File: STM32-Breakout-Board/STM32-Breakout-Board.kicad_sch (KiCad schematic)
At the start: 1 part, among them U1 stm32l443cct6

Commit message: Schematic and Layout update
Finished the first draft of the Schematic.
Started layout
Edited some components
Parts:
- added C1, C2, C3, C4, C9: 100n, Capacitor_SMD:C_0402_1005Metric, symbol Device:C
- added C10, C11: 10p, Capacitor_SMD:C_0402_1005Metric, symbol Device:C
- added C12, C13: 22u, Capacitor_SMD:C_0805_2012Metric, symbol Device:C
- added C5: 10u, Capacitor_SMD:C_0805_2012Metric, symbol Device:C
- added C6: 10n, Capacitor_SMD:C_0402_1005Metric, symbol Device:C
- added C7, C8: 1u, Capacitor_SMD:C_0603_1608Metric, symbol Device:C
- added D1: RED, LED_SMD:LED_0603_1608Metric, symbol Device:LED
- added FB1: 120R, Inductor_SMD:L_0603_1608Metric, symbol Device:FerriteBead
- added H1, H2, H3, H4: MountingHole, MountingHole:MountingHole_2.5mm, symbol Mechanical:MountingHole
- added J1: USB_B_Micro, Connector_USB:USB_Micro-B_Wuerth_629105150521, symbol Connector:USB_B_Micro
- added J2: Conn_01x04_Pin, Connector_PinSocket_2.00mm:PinSocket_1x04_P2.00mm_Vertical, symbol Connector:Conn_01x04_Pin
- added J3, J4: Conn_01x10_Socket, Connector_PinSocket_2.00mm:PinSocket_1x10_P2.00mm_Vertical, symbol Connector:Conn_01x10_Socket
- added R1, R2, R3, R4, R5: 1k5, Resistor_SMD:R_0402_1005Metric, symbol Device:R
- added SW1: SW_SPDT, Button_Switch_SMD:SW_SPDT_PCM12, symbol Switch:SW_SPDT
- added U2: MCP1799T-3302H/DB, BBSTM32_pcblib:SOT-223 b, symbol BBSTM32_symlib:MCP1799T-3302H/DB
- added Y1: Crystal_GND24, Crystal:Crystal_SMD_3225-4Pin_3.2x2.5mm, symbol Device:Crystal_GND24
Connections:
- net +3.3V: now reaches U1.1 (VBAT)
- net +3.3V: now also U1.24 (VDD), U1.36 (VDDUSB), U1.48 (VDD), C1.1, C13.1, C2.1, C3.1, C4.1, C5.1, C8.1, FB1.2, J2.1 (Pin_1), R2.2, R3.2, R4.1, R5.2, SW1.3 (C), U2.3 (VOUT)
- net PA0: now reaches U1.10 (PA0)
- net PA0: now also J3.1 (Pin_1)
- net PA1: now reaches U1.11 (PA1)
- net PA1: now also J3.2 (Pin_2)
- net PA2: now reaches U1.12 (PA2)
- net PA2: now also J3.3 (Pin_3)
- net PA3: now reaches U1.13 (PA3)
- net PA3: now also J3.4 (Pin_4)
- net PA4: now reaches U1.14 (PA4)
- net PA4: now also J3.5 (Pin_5)
- net PA5: now reaches U1.15 (PA5)
- net PA5: now also J3.6 (Pin_6)
- net PA6: now reaches U1.16 (PA6)
- net PA6: now also J3.7 (Pin_7)
- net PA7: now reaches U1.17 (PA7)
- net PA7: now also J3.8 (Pin_8)
- net PB0: now reaches U1.18 (PB0)
- net PB0: now also J4.1 (Pin_1)
- net PB1: now reaches U1.19 (PB1)
- net PB1: now also J4.2 (Pin_2)
- net PB2: now reaches U1.20 (PB2)
- net PB2: now also J4.3 (Pin_3)
- net I2C_SCL: now reaches U1.21 (PB10)
- net I2C_SCL: now also J2.2 (Pin_2), R2.1
- net I2C_SDA: now reaches U1.22 (PB11)
- net I2C_SDA: now also J2.3 (Pin_3), R3.1
- net GND: now reaches U1.23 (VSS)
- net GND: now also U1.35 (VSS), U1.47 (VSS), U1.8 (VSSA), C1.2, C10.2, C11.2, C12.2, C13.2, C2.2, C3.2, C4.2, C5.2, C6.2, C7.2, C8.2, C9.1, D1.1 (K), J1.5 (GND), J2.4 (Pin_4), SW1.1 (A), U2.2 (GND), Y1.2 (G), Y1.4 (G)
- net PA8: now reaches U1.29 (PA8)
- net PA8: now also J3.9 (Pin_9)
- net PA9: now reaches U1.30 (PA9)
- net PA9: now also J3.10 (Pin_10)
- net USB_D-: now reaches U1.32 (PA11)
- net USB_D-: now also J1.2 (D-)
- net USB_D+: now reaches U1.33 (PA12)
- net USB_D+: now also J1.3 (D+), R5.1
- net PB3: now reaches U1.39 (PB3)
- net PB3: now also J4.4 (Pin_4)
- net PB4: now reaches U1.40 (PB4)
- net PB4: now also J4.5 (Pin_5)
- net PB5: now reaches U1.41 (PB5)
- net PB5: now also J4.6 (Pin_6)
- net PB6: now reaches U1.42 (PB6)
- net PB6: now also J4.7 (Pin_7)
- net PB7: now reaches U1.43 (PB7)
- net PB7: now also J4.8 (Pin_8)
- net BOOT0: now reaches U1.44 (BOOT0)
- net BOOT0: now also R1.2
- net PB8: now reaches U1.45 (PB8)
- net PB8: now also J4.9 (Pin_9)
- net PB9: now reaches U1.46 (PB9)
- net PB9: now also J4.10 (Pin_10)
- net HSE_IN: now reaches U1.5 (PH0)
- net HSE_IN: now also C10.1, Y1.1
- net HSE_OUT: now reaches U1.6 (PH1)
- net HSE_OUT: now also C11.1, Y1.3
- net NRST: now reaches U1.7 (NRST)
- net NRST: now also C9.2
- net +3.3VA: now reaches U1.9 (VDDA)
- net +3.3VA: now also C6.1, C7.1, FB1.1
- new net LED_A: D1.2 (A), R4.2
- new net SW_BOOT0: R1.1, SW1.2 (B)
- new net VBUS: C12.1, J1.1 (VBUS), U2.1 (VIN)
- no-connect marks 0 -> 13
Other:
- note added: "I2C and USB"
- note added: "Microcontroller"
- note added: "Mounting Holes"
- note added: "Power Supply"
- note added: "STM32 Breakout Board"
- company: (none) -> SaintDTS
- title: (none) -> STM32 Breakout Board

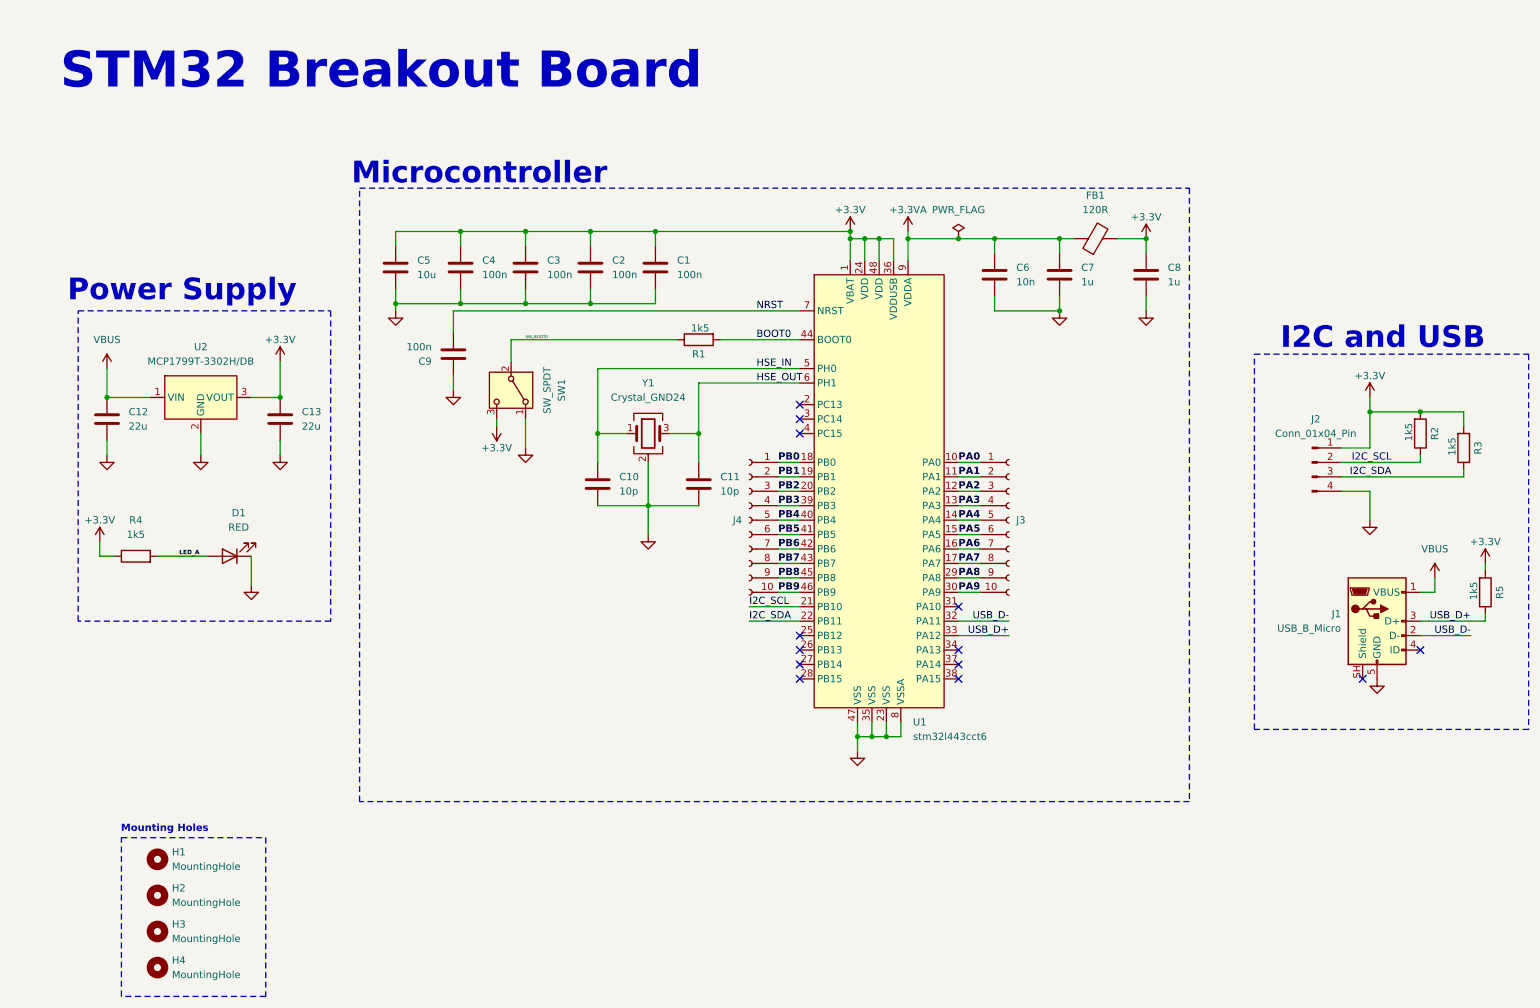
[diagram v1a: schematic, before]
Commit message: Update on schematics
Changed the connector type from socket to pin.
Changed the order in which pins are connected
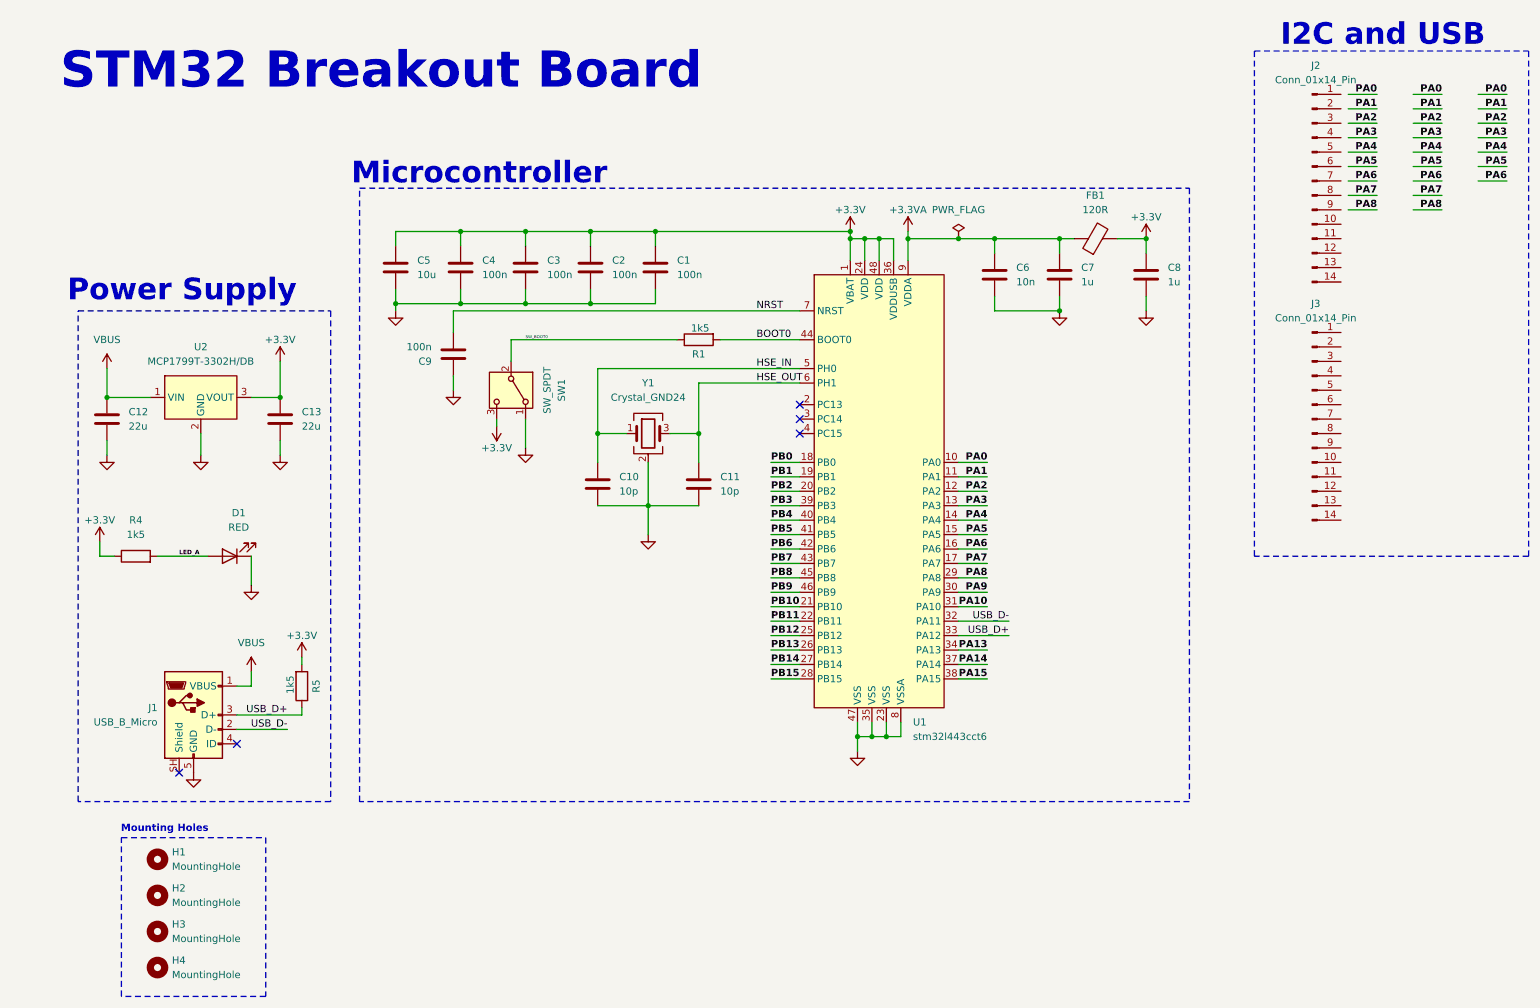
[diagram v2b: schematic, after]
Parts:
- removed J2: Conn_01x04_Pin, Connector_PinSocket_2.00mm:PinSocket_1x04_P2.00mm_Vertical, symbol Connector:Conn_01x04_Pin
- removed J3, J4: Conn_01x10_Socket, Connector_PinSocket_2.00mm:PinSocket_1x10_P2.00mm_Vertical, symbol Connector:Conn_01x10_Socket
- removed R2, R3: 1k5, Resistor_SMD:R_0402_1005Metric, symbol Device:R
- added J2, J3: Conn_01x14_Pin, symbol Connector:Conn_01x14_Pin
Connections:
- net PB12: now reaches U1.25 (PB12)
- net PB13: now reaches U1.26 (PB13)
- net PB14: now reaches U1.27 (PB14)
- net PB15: now reaches U1.28 (PB15)
- net PA10: now reaches U1.31 (PA10)
- net PA13: now reaches U1.34 (PA13)
- net PA14: now reaches U1.37 (PA14)
- net PA15: now reaches U1.38 (PA15)
- net I2C_SCL renamed PB10
- net I2C_SDA renamed PB11
- no-connect marks 13 -> 5
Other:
- moved on the sheet: J1, R5

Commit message: Final Update
Completed layout and Silkscreen decoration
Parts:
- removed J2, J3: Conn_01x14_Pin, symbol Connector:Conn_01x14_Pin
- removed R5: 1k5, Resistor_SMD:R_0402_1005Metric, symbol Device:R
- added J2, J3: Conn_01x20_Pin, Connector_PinHeader_2.54mm:PinHeader_1x20_P2.54mm_Vertical, symbol Connector:Conn_01x20_Pin
- C1, C2, C3, C4, C9: Distributor 1 (none) -> https://eu.mouser.com/en/ProductDetail/KYOCERA-AVX/04025C10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; Manufacturer (none) -> KYOCERA AVX; Part Number (none) -> 04025C104JAT2A
- C10, C11: Distributor 1 (none) -> https://eu.mouser.com/en/ProductDetail/KYOCERA-AVX/KGM05ACG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; Manufacturer (none) -> KYOCERA AVX; Part Number (none) -> KGM05ACG1H100JH
- C12, C13: Distributor 1 (none) -> https://eu.mouser.com/en/ProductDetail/KYOCERA-AVX/KGM21AR5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; Manufacturer (none) -> KYOCERA AVX; Part Number (none) -> KGM21AR51C226KU
- C5: Distributor 1 (none) -> https://eu.mouser.com/en/ProductDetail/TDK/CGA4J1X7R0J106K1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; Manufacturer (none) -> TDK; Part Number (none) -> CGA4J1X7R0J106K125AC
- C6: Distributor 1 (none) -> https://eu.mouser.com/en/ProductDetail/KYOCERA-AVX/KAM05AR7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; Manufacturer (none) -> KYOCERA AVX; Part Number (none) -> KAM05AR71C103JH
- C7, C8: Distributor 1 (none) -> https://eu.mouser.com/en/ProductDetail/KYOCERA-AVX/KGM15BR7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; Manufacturer (none) -> KYOCERA AVX; Part Number (none) -> KGM15BR71C105JT
- D1: Distributor 1 (none) -> https://eu.mouser.com/en/ProductDetail/Vishay-Semiconductor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; Manufacturer (none) -> Vishay Semiconductors; Part Number (none) -> TLMS1000-GS15
- FB1: Distributor 1 (none) -> https://eu.mouser.com/en/ProductDetail/Murata-Electronics/B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; Manufacturer (none) -> Murata Electronics; Part Number (none) -> BLM18BD121SH1D
- J1: Distributor 1 (none) -> https://eu.mouser.com/en/ProductDetail/Wurth-Elektronik/629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; Manufacturer (none) -> Wurth Elektronik; Part Number (none) -> 629105150521
- R1, R4: Distributor 1 (none) -> https://eu.mouser.com/en/ProductDetail/Royalohm/CQ02WGJ0152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; Manufacturer (none) -> Royalohm; Part Number (none) -> CQ02WGJ0152TCE
- SW1: Distributor 1 (none) -> https://eu.mouser.com/en/ProductDetail/SparkFun/COM-09609?q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; Manufacturer (none) -> SparkFun; Part Number (none) -> COM-09609
- U1: Distributor 1 (none) -> https://eu.mouser.com/en/ProductDetail/STMicroelectronics/S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; Manufacturer (none) -> STMicroelectronics; Part Number (none) -> stm32l443cct6
- U2: Distributor 1 (none) -> https://eu.mouser.com/en/ProductDetail/Microchip-Technology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; Manufacturer (none) -> Microchip Technology; Part Number (none) -> MCP1799-5002H/DB
- Y1: Distributor 1 (none) -> https://eu.mouser.com/en/ProductDetail/KYOCERA-AVX/CX3225CA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; Manufacturer (none) -> KYOCERA AVX; Part Number (none) -> CX3225CA12000F0KFQCC
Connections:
- net +3.3V: now also J2.8 (Pin_8)
- net GND: now also J2.1 (Pin_1), J2.9 (Pin_9), J3.10 (Pin_10)
- net PA0: now also J2.5 (Pin_5)
- net PA1: now also J2.6 (Pin_6)
- net PA10: now also J3.14 (Pin_14)
- net PA13: now also J3.11 (Pin_11)
- net PA14: now also J3.9 (Pin_9)
- net PA15: now also J3.8 (Pin_8)
- net PA2: now also J2.7 (Pin_7)
- net PA3: now also J2.10 (Pin_10)
- net PA4: now also J2.11 (Pin_11)
- net PA5: now also J2.12 (Pin_12)
- net PA6: now also J2.13 (Pin_13)
- net PA7: now also J2.14 (Pin_14)
- net PA8: now also J3.16 (Pin_16)
- net PA9: now also J3.15 (Pin_15)
- net PB0: now also J2.15 (Pin_15)
- net PB1: now also J2.16 (Pin_16)
- net PB10: now also J2.18 (Pin_18)
- net PB11: now also J2.19 (Pin_19)
- net PB12: now also J3.20 (Pin_20)
- net PB13: now also J3.19 (Pin_19)
- net PB14: now also J3.18 (Pin_18)
- net PB15: now also J3.17 (Pin_17)
- net PB2: now also J2.17 (Pin_17)
- net PB3: now also J3.7 (Pin_7)
- net PB4: now also J3.6 (Pin_6)
- net PB5: now also J3.5 (Pin_5)
- net PB6: now also J3.4 (Pin_4)
- net PB7: now also J3.3 (Pin_3)
- net PB8: now also J3.2 (Pin_2)
- net PB9: now also J3.1 (Pin_1)
- net VBUS: now also J2.20 (Pin_20)
- net PC13: now reaches U1.2 (PC13)
- net PC13: now also J2.2 (Pin_2)
- net PC14: now reaches U1.3 (PC14)
- net PC14: now also J2.3 (Pin_3)
- net PC15: now reaches U1.4 (PC15)
- net PC15: now also J2.4 (Pin_4)
- net USB_D+: no longer names the net of J1.3 (D+)
- net USB_D+: no longer U1.33 (PA12)
- net USB_D-: no longer names the net of J1.2 (D-)
- net USB_D-: no longer U1.32 (PA11)
- new net PA11: J3.13 (Pin_13), U1.32 (PA11)
- new net PA12: J3.12 (Pin_12), U1.33 (PA12)
- no-connect marks 5 -> 4
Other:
- note added: "Connectors"
- note removed: "I2C and USB"

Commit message: Edited BOM
Added a price column to the BOM
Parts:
- C1, C2, C3, C4, C9: Price (none) -> $0.13
- C10, C11, FB1: Price (none) -> $0.10
- C12, C13: Price (none) -> $0.48
- C5: Price (none) -> $0.27
- C6: Price (none) -> $0.12
- C7, C8: Price (none) -> $0.28
- D1, U2: Price (none) -> $0.42
- J1: Price (none) -> $2.21
- J2, J3: Price (none) -> $0.68
- R1, R4: Price (none) -> $0.003
- SW1: Price (none) -> $0.95
- U1: Price (none) -> $5.79
- Y1: Price (none) -> $0.54
